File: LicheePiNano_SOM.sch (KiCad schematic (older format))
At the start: 1 part

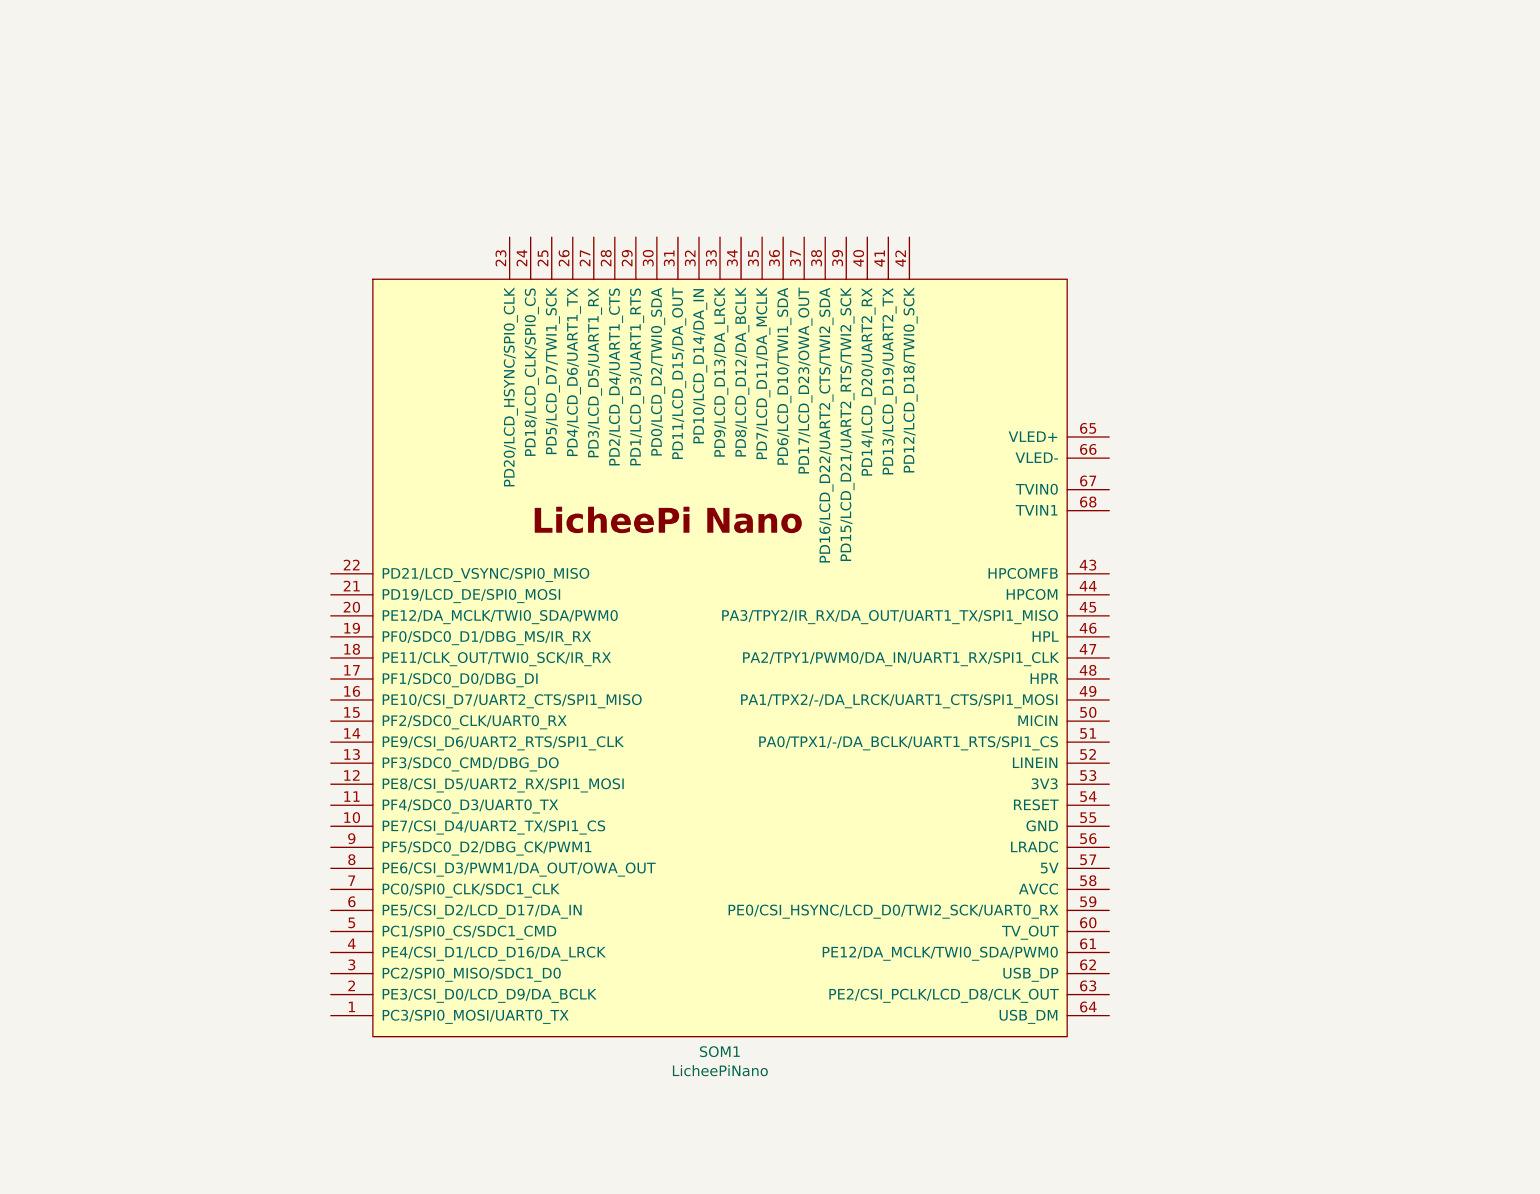
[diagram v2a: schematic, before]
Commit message: Added WiFi and figurated some components on pcb
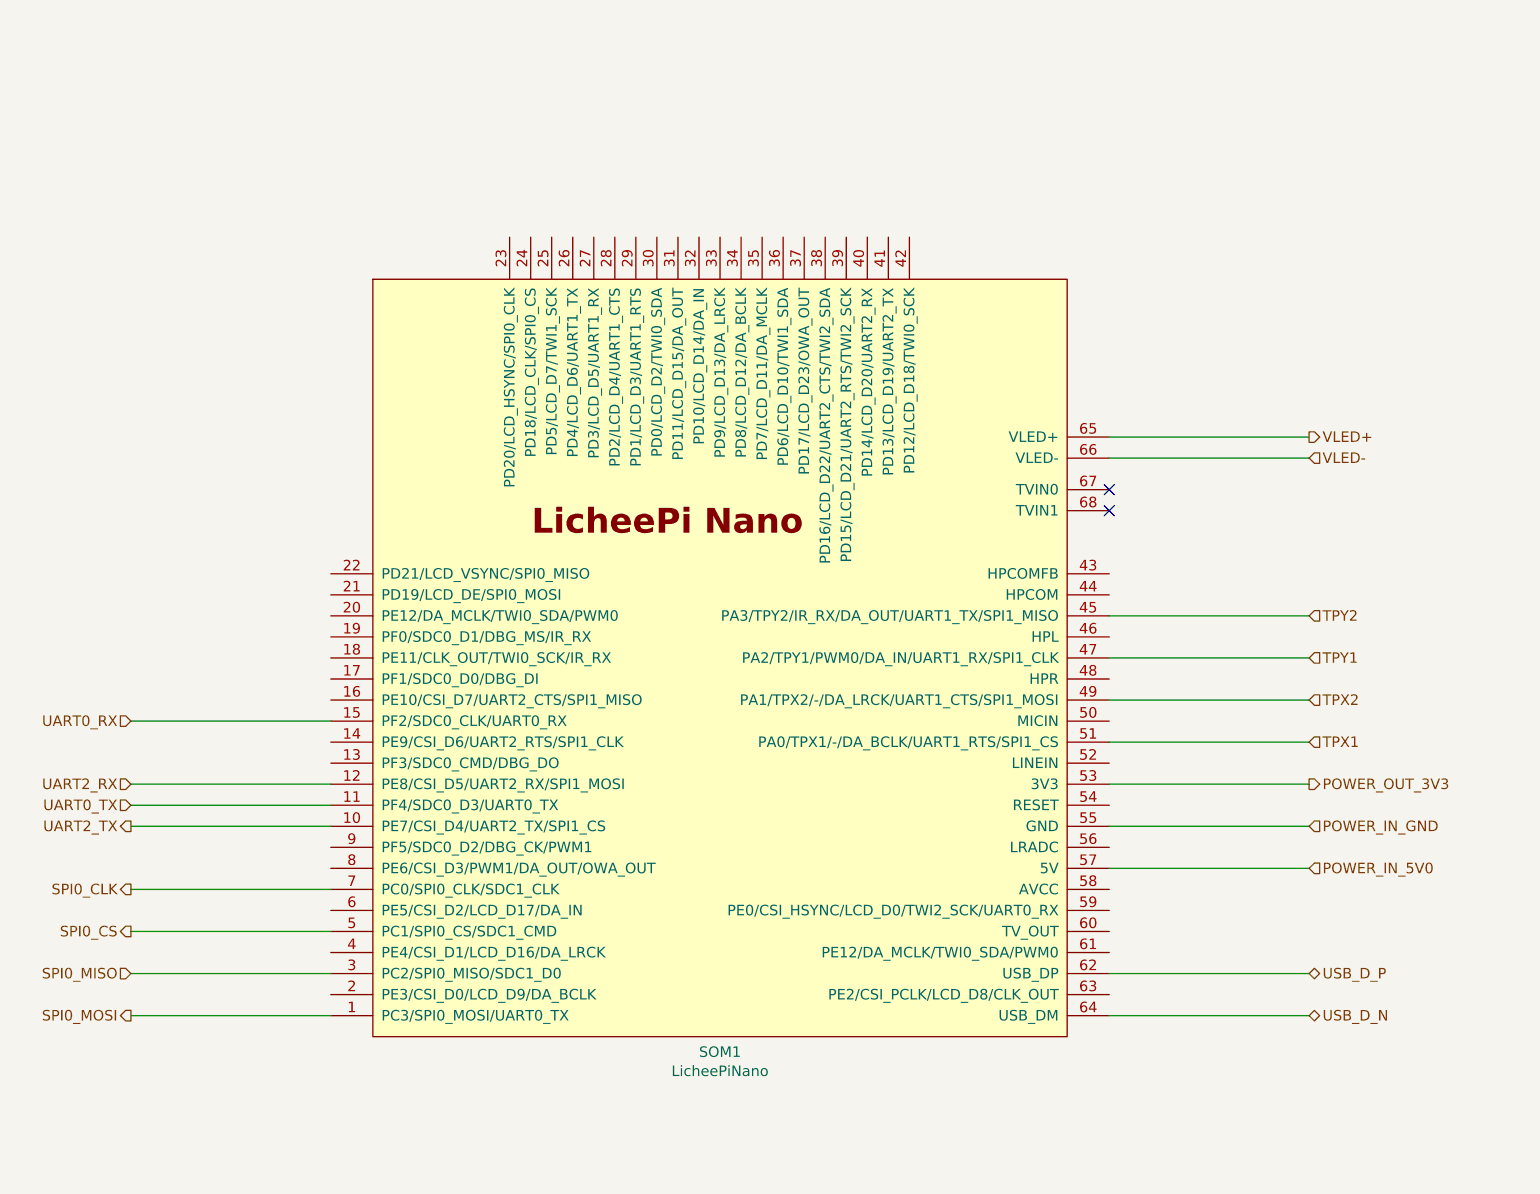
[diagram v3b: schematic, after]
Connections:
- net SPI0_MOSI: now reaches SOM1.1 (PC3/SPI0_MOSI/UART0_TX)
- net UART2_TX: now reaches SOM1.10 (PE7/CSI_D4/UART2_TX/SPI1_CS)
- net UART0_TX: now reaches SOM1.11 (PF4/SDC0_D3/UART0_TX)
- net UART2_RX: now reaches SOM1.12 (PE8/CSI_D5/UART2_RX/SPI1_MOSI)
- net UART0_RX: now reaches SOM1.15 (PF2/SDC0_CLK/UART0_RX)
- net SPI0_MISO: now reaches SOM1.3 (PC2/SPI0_MISO/SDC1_D0)
- net TPY2: now reaches SOM1.45 (PA3/TPY2/IR_RX/DA_OUT/UART1_TX/SPI1_MISO)
- net TPY1: now reaches SOM1.47 (PA2/TPY1/PWM0/DA_IN/UART1_RX/SPI1_CLK)
- net TPX2: now reaches SOM1.49 (PA1/TPX2/-/DA_LRCK/UART1_CTS/SPI1_MOSI)
- net SPI0_CS: now reaches SOM1.5 (PC1/SPI0_CS/SDC1_CMD)
- net TPX1: now reaches SOM1.51 (PA0/TPX1/-/DA_BCLK/UART1_RTS/SPI1_CS)
- net POWER_OUT_3V3: now reaches SOM1.53 (3V3)
- net POWER_IN_GND: now reaches SOM1.55 (GND)
- net POWER_IN_5V0: now reaches SOM1.57 (5V)
- net USB_D_P: now reaches SOM1.62 (USB_DP)
- net USB_D_N: now reaches SOM1.64 (USB_DM)
- net VLED+: now reaches SOM1.65 (VLED+)
- net VLED-: now reaches SOM1.66 (VLED-)
- net SPI0_CLK: now reaches SOM1.7 (PC0/SPI0_CLK/SDC1_CLK)
- no-connect marks 0 -> 2
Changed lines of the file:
@@
 $Descr A3 16535 11693
 encoding utf-8
-Sheet 2 8
+Sheet 2 10
 Title "LicheePi Nano SOM"
 Date "2020-11-14"
@@
 	1    0    0    -1
 $EndComp
+Wire Wire Line
+	9700 4300 10650 4300
+Wire Wire Line
+	9700 4400 10650 4400
+Text HLabel 10650 4300 2    50   Output ~ 0
+VLED+
+Text HLabel 10650 4400 2    50   Input ~ 0
+VLED-
+NoConn ~ 9700 4550
+NoConn ~ 9700 4650
+Wire Wire Line
+	9700 5750 10650 5750
+Wire Wire Line
+	9700 5550 10650 5550
+Wire Wire Line
+	9700 5350 10650 5350
+Wire Wire Line
+	9700 5150 10650 5150
+Text HLabel 10650 5150 2    50   Input ~ 0
+TPY2
+Text HLabel 10650 5350 2    50   Input ~ 0
+TPY1
+Text HLabel 10650 5550 2    50   Input ~ 0
+TPX2
+Text HLabel 10650 5750 2    50   Input ~ 0
+TPX1
+Wire Wire Line
+	9700 5950 10650 5950
+Wire Wire Line
+	9700 6150 10650 6150
+Wire Wire Line
+	9700 6350 10650 6350
+Text HLabel 10650 5950 2    50   Output ~ 0
+POWER_OUT_3V3
+Text HLabel 10650 6350 2    50   Input ~ 0
+POWER_IN_5V0
+Text HLabel 10650 6150 2    50   Input ~ 0
+POWER_IN_GND
+Wire Wire Line
+	9700 7050 10650 7050
+Wire Wire Line
+	9700 6850 10650 6850
+Text HLabel 10650 6850 2    50   BiDi ~ 0
+USB_D_P
+Text HLabel 10650 7050 2    50   BiDi ~ 0
+USB_D_N
+Wire Wire Line
+	5050 7050 6000 7050
+Text HLabel 5050 7050 0    50   Output ~ 0
+SPI0_MOSI
+Wire Wire Line
+	5050 6850 6000 6850
+Text HLabel 5050 6850 0    50   Input ~ 0
+SPI0_MISO
+Wire Wire Line
+	5050 6650 6000 6650
+Text HLabel 5050 6650 0    50   Output ~ 0
+SPI0_CS
+Wire Wire Line
+	5050 6450 6000 6450
+Text HLabel 5050 6450 0    50   Output ~ 0
+SPI0_CLK
+Wire Wire Line
+	5050 6150 6000 6150
+Text HLabel 5050 6150 0    50   Output ~ 0
+UART2_TX
+Wire Wire Line
+	5050 5950 6000 5950
+Text HLabel 5050 5950 0    50   Input ~ 0
+UART2_RX
+Wire Wire Line
+	5050 6050 6000 6050
+Text HLabel 5050 6050 0    50   Input ~ 0
+UART0_TX
+Wire Wire Line
+	5050 5650 6000 5650
+Text HLabel 5050 5650 0    50   Input ~ 0
+UART0_RX
 $EndSCHEMATC

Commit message: Schematic finished, with check ERC
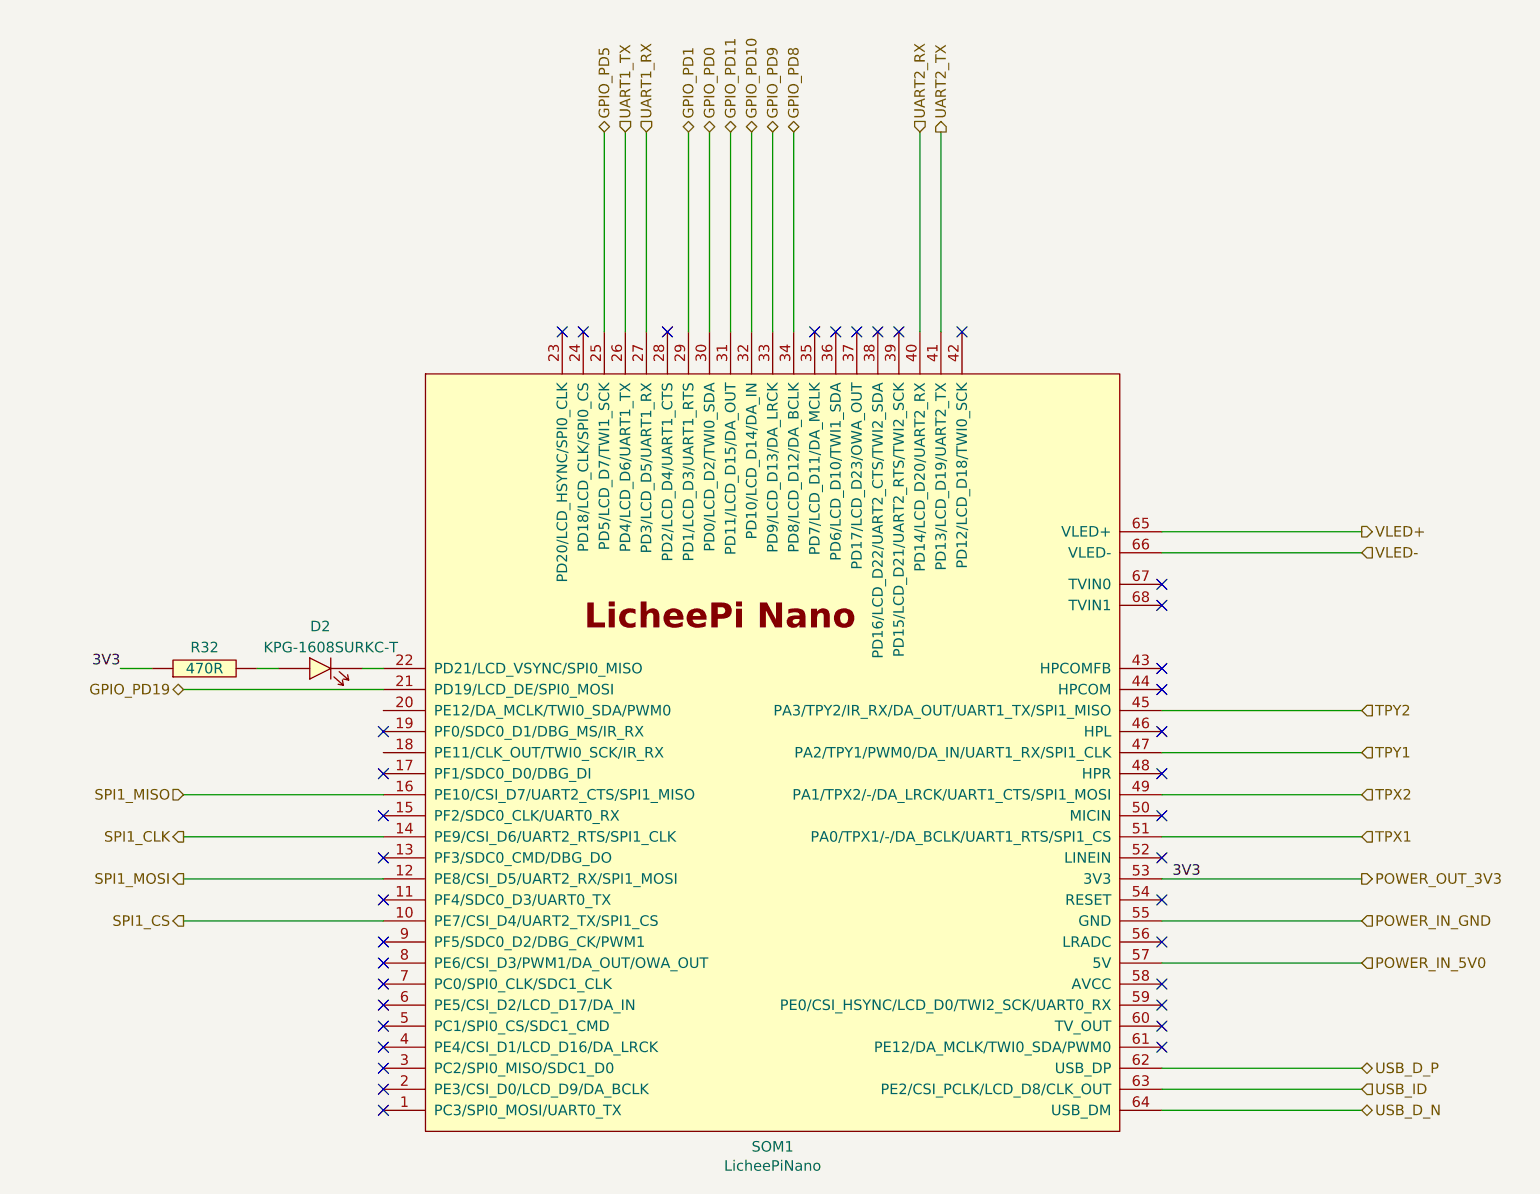
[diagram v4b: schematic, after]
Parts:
- added D2: KPG-1608SURKC-T, Diodes:LED_KPG-1608SURKC-T, symbol Diodes:KPG-1608SURKC-T
- added R32: 470R, Resistor_Smd_0402:470R_0402, symbol Resistors_Smd0402:470R_0402
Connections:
- net POWER_OUT_3V3: now also R32.1
- net UART2_RX: now also SOM1.40 (PD14/LCD_D20/UART2_RX); no longer SOM1.12 (PE8/CSI_D5/UART2_RX/SPI1_MOSI)
- net UART2_TX: now also SOM1.41 (PD13/LCD_D19/UART2_TX); no longer SOM1.10 (PE7/CSI_D4/UART2_TX/SPI1_CS)
- net SPI1_CLK: now reaches SOM1.14 (PE9/CSI_D6/UART2_RTS/SPI1_CLK)
- net SPI1_MISO: now reaches SOM1.16 (PE10/CSI_D7/UART2_CTS/SPI1_MISO)
- net GPIO_PD19: now reaches SOM1.21 (PD19/LCD_DE/SPI0_MOSI)
- net at SOM1.22 (PD21/LCD_VSYNC/SPI0_MISO): now also D2.2 (K)
- net GPIO_PD5: now reaches SOM1.25 (PD5/LCD_D7/TWI1_SCK)
- net UART1_TX: now reaches SOM1.26 (PD4/LCD_D6/UART1_TX)
- net UART1_RX: now reaches SOM1.27 (PD3/LCD_D5/UART1_RX)
- net GPIO_PD1: now reaches SOM1.29 (PD1/LCD_D3/UART1_RTS)
- net GPIO_PD0: now reaches SOM1.30 (PD0/LCD_D2/TWI0_SDA)
- net GPIO_PD11: now reaches SOM1.31 (PD11/LCD_D15/DA_OUT)
- net GPIO_PD10: now reaches SOM1.32 (PD10/LCD_D14/DA_IN)
- net GPIO_PD9: now reaches SOM1.33 (PD9/LCD_D13/DA_LRCK)
- net GPIO_PD8: now reaches SOM1.34 (PD8/LCD_D12/DA_BCLK)
- net USB_ID: now reaches SOM1.63 (PE2/CSI_PCLK/LCD_D8/CLK_OUT)
- net SPI0_CLK: no longer names the net of SOM1.7 (PC0/SPI0_CLK/SDC1_CLK)
- net SPI0_CS: no longer names the net of SOM1.5 (PC1/SPI0_CS/SDC1_CMD)
- net SPI0_MISO: no longer names the net of SOM1.3 (PC2/SPI0_MISO/SDC1_D0)
- net SPI0_MOSI: no longer names the net of SOM1.1 (PC3/SPI0_MOSI/UART0_TX)
- net UART0_RX: no longer names the net of SOM1.15 (PF2/SDC0_CLK/UART0_RX)
- net UART0_TX: no longer names the net of SOM1.11 (PF4/SDC0_D3/UART0_TX)
- new net: D2.1 (A), R32.2
- new net SPI1_CS: SOM1.10 (PE7/CSI_D4/UART2_TX/SPI1_CS)
- new net SPI1_MOSI: SOM1.12 (PE8/CSI_D5/UART2_RX/SPI1_MOSI)
- no-connect marks 2 -> 37
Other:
- moved on the sheet: SOM1
